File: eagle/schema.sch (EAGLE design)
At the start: 8 parts, among them IC1 PICAXE-08M2-DIL, K1 ARK500/2

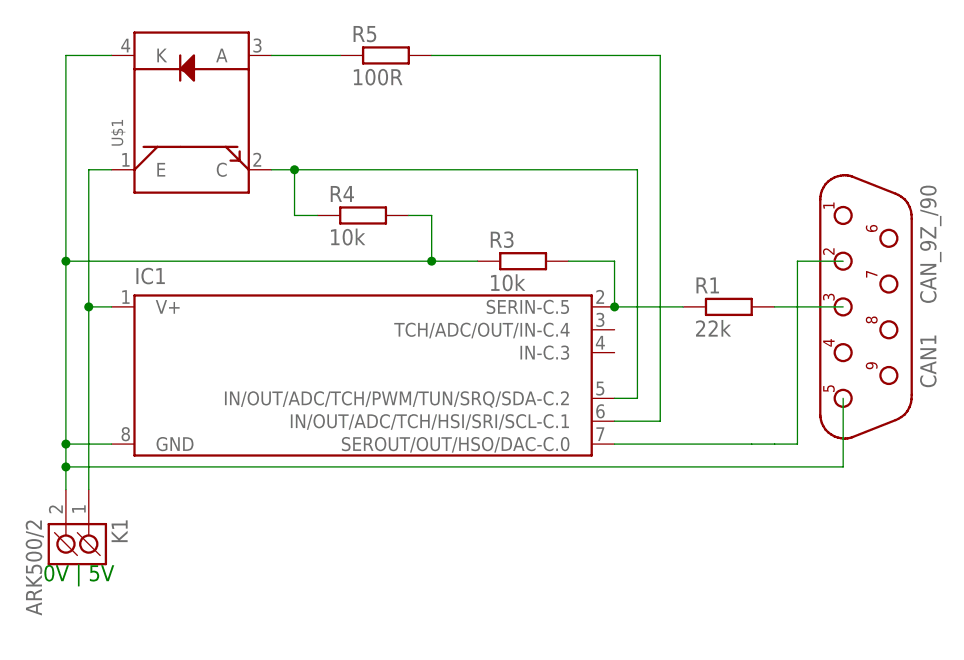
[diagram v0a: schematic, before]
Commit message: [Eagle] Removed surplus layers, packages and symbols
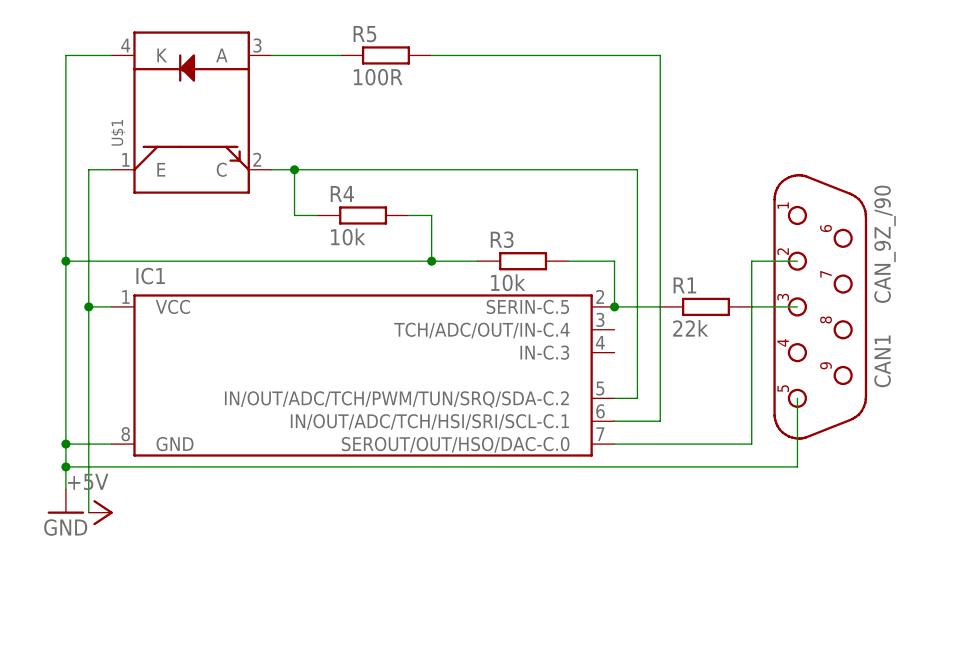
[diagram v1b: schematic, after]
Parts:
- removed K1: ARK500/2, #PaJa_konektory:ARK500/2
- CAN1: device #PaJa_konektory:CAN_9Z_/90 -> RONJA:CAN_9Z_/90
- R1, R3, R4, R5: device eagle-ltspice:R0207/10 -> RONJA:R0207/10
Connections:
- removed net N$7: CAN1.5, IC1.GND@8, K1.K2, R3.1, R4.2, U$1.K
- removed net N$9: IC1.V+@1, K1.K1, U$1.E
- new net +5V: IC1.VCC@1, U$1.E
- new net GND: CAN1.5, IC1.GND@8, R3.1, R4.2, U$1.K
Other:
- note removed: "0V | 5V"
- moved on the sheet: CAN1, R1

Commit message: [Eagle] Minified schema
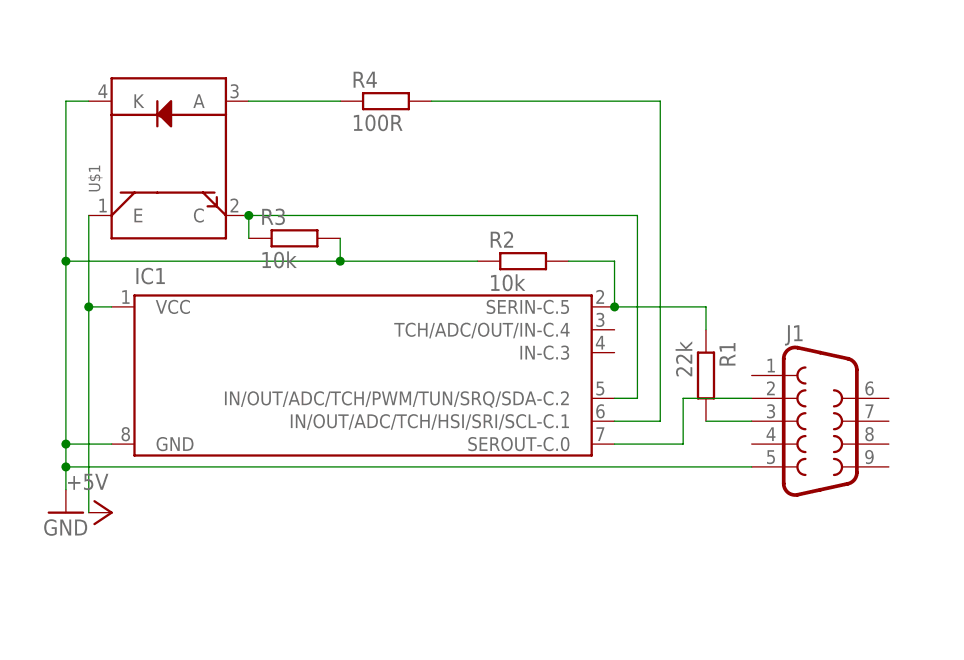
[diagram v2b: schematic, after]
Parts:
- removed CAN1: CAN_9Z_/90, RONJA:CAN_9Z_/90
- removed R5: 100R, RONJA:R0207/10
- added J1: (no value), SparkFun-Connectors:DB9FEMALE
- added R2: 10k, RONJA:R0207/10
- R4: value 10k -> 100R
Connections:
- net GND: now also J1.5, R2.1, R3.2; no longer CAN1.5, R3.1, R4.2
- net N$1: now also IC1.SEROUT-C.0@7, J1.2; no longer CAN1.2, IC1.SEROUT/OUT/HSO/DAC-C.0@7
- net N$10: now also R2.2; no longer R3.2
- net N$2: now also J1.3; no longer CAN1.3
- net N$4: now also R4.1; no longer R5.1
- net N$5: now also R4.2; no longer R5.2
- net N$6: now also R3.1; no longer R4.1
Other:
- moved on the sheet: R1, R3, R4, U$1
